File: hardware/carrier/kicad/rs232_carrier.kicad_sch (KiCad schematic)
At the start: 45 parts, among them J1 WS header 1-14, J2 WS header 15-28, J3 EXT, Q11 2N7002, Q12 AO3401A, Q21 2N7002, Q22 AO3401A, Q31 2N7002, Q32 AO3401A, Q41 2N7002, Q42 AO3401A, U5 MT3608

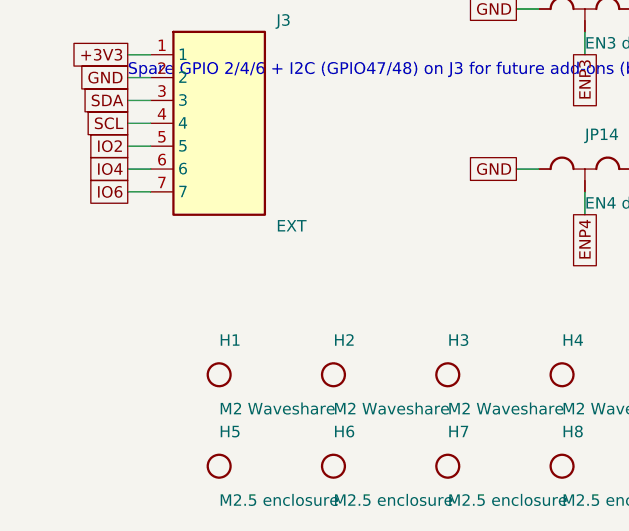
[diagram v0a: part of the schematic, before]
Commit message: Hardware 0.2: Modul hochkant, Gehäuse zum Zusammenstecken, Akkuklappe
Trägerplatine 78 × 107 mm: Waveshare-Modul hochkant mit USB-C an der
Stirnseite, Versorgung daneben, JST-PH für den Akku auf der Unterseite.
Gehäuse aus drei Teilen ohne Schrauben: Lippe/Nut, vier lösbare Rasthaken,
Pfosten klemmen die Platine, Displayglas als Oberseite, Akkuklappe mit
Rastlasche. Neu geroutet, KiCad-DRC ohne elektrische Fehler.

Co-Authored-By: Claude Fable 5.1 <noreply@anthropic.com>
Claude-Session: https://claude.ai/code/session_01NzB9JfE6QfygfS2yw734Lm
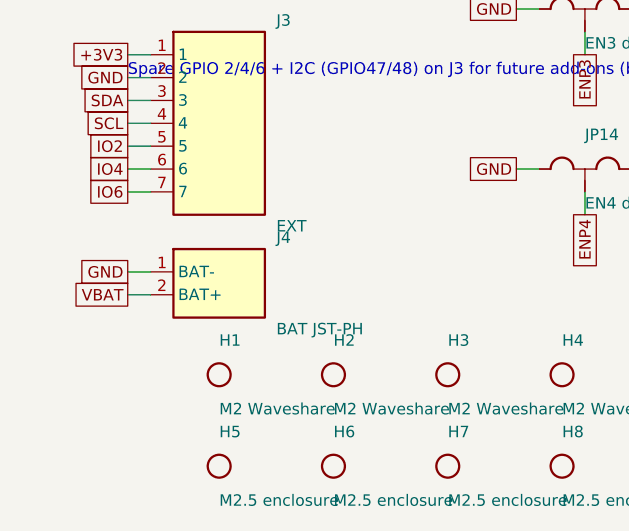
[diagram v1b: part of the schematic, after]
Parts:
- added J4: BAT JST-PH, rs232fp:JST_PH_2_Vertical, symbol rs232:Conn_1x2
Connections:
- net GND: now also J4.1 (BAT-)
- net VBAT: now also J4.2 (BAT+)
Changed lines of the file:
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@@
     (property "Intersheetrefs" "${INTERSHEET_REFS}" (at 182.88 163.83 0) (effects (font (size 1.27 1.27)) hide))
+  )
+  (symbol (lib_id "rs232:Conn_1x2") (at 30.48 175.26 0) (unit 1)
+    (in_bom yes) (on_board yes) (dnp no) (fields_autoplaced)
+    (property "Reference" "J4" (at 36.83 170.18 0) (effects (font (size 1.27 1.27)) (justify left)))
+    (property "Value" "BAT JST-PH" (at 36.83 180.34 0) (effects (font (size 1.27 1.27)) (justify left)))
+    (property "Footprint" "rs232fp:JST_PH_2_Vertical" (at 30.48 175.26 0) (effects (font (size 1.27 1.27)) hide))
+    (property "Datasheet" "" (at 30.48 175.26 0) (effects (font (size 1.27 1.27)) hide))
+    (property "Note" "battery, bottom side (in the battery bay). VBAT reaches the module through header pin 14 - verify that pin is the cell terminal" (at 30.48 175.26 0) (effects (font (size 1.27 1.27)) hide))
+    (pin "1")
+    (pin "2")
+    (instances (project "rs232_carrier"
+      (path "/1a0da8ea-64fd-5a8d-a1fa-9a98526e6966" (reference "J4") (unit 1))
+    ))
+  )
+  (wire (pts (xy 22.86 173.99) (xy 20.32 173.99)) (stroke (width 0) (type default)))
+  (global_label "GND" (shape passive) (at 20.32 173.99 180) (fields_autoplaced) (effects (font (size 1.27 1.27)) (justify right))
+    (property "Intersheetrefs" "${INTERSHEET_REFS}" (at 20.32 173.99 0) (effects (font (size 1.27 1.27)) hide))
+  )
+  (wire (pts (xy 22.86 176.53) (xy 20.32 176.53)) (stroke (width 0) (type default)))
+  (global_label "VBAT" (shape passive) (at 20.32 176.53 180) (fields_autoplaced) (effects (font (size 1.27 1.27)) (justify right))
+    (property "Intersheetrefs" "${INTERSHEET_REFS}" (at 20.32 176.53 0) (effects (font (size 1.27 1.27)) hide))
   )
   (symbol (lib_id "rs232:MountingHole") (at 30.48 185.42 0) (unit 1)
